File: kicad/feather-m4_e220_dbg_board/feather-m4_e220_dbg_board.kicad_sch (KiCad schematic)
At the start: 2 parts, among them U1 FEATHER_M4*, U2 E220

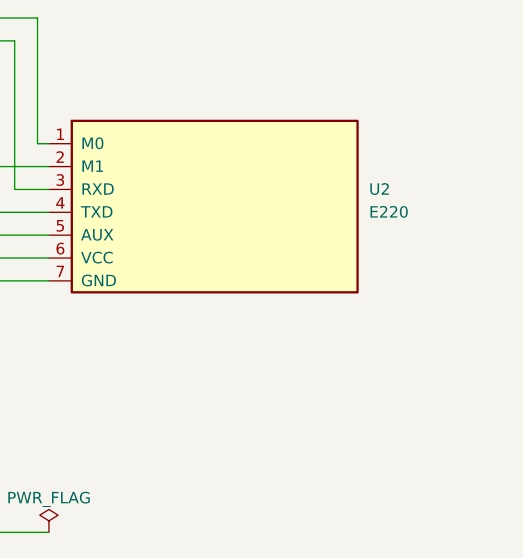
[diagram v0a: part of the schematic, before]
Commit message: Changed to place through holes for remaining E220 (as Pin8-9)
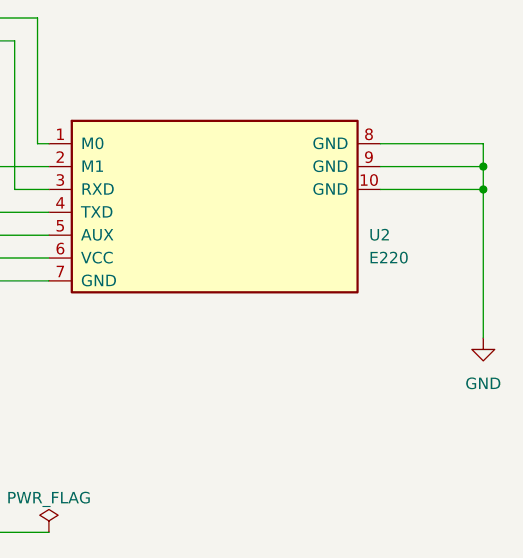
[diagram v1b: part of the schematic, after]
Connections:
- net GND: now also U2.10 (GND), U2.8 (GND), U2.9 (GND)
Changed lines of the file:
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@@
   (title_block
     (title "E220 - Feather debug board")
-    (date "2023-02-23")
-    (rev "0.1.0")
+    (date "2023-02-27")
+    (rev "0.1.1")
+  )
+  (junction (at 223.52 80.01) (diameter 0) (color 0 0 0 0)
   )
   (junction (at 165.1 120.65) (diameter 0) (color 0 0 0 0)
+  )
+  (junction (at 223.52 82.55) (diameter 0) (color 0 0 0 0)
   )
   (no_connect (at 149.86 80.01))
@@
     (stroke (width 0) (type default))
   )
+  (wire (pts (xy 223.52 82.55) (xy 223.52 99.06))
+    (stroke (width 0) (type default))
+  )
   (wire (pts (xy 173.99 63.5) (xy 173.99 77.47))
     (stroke (width 0) (type default))
@@
     (stroke (width 0) (type default))
   )
+  (wire (pts (xy 223.52 77.47) (xy 223.52 80.01))
+    (stroke (width 0) (type default))
+  )
   (wire (pts (xy 165.1 92.71) (xy 175.26 92.71))
     (stroke (width 0) (type default))
@@
     (stroke (width 0) (type default))
   )
+  (wire (pts (xy 212.09 82.55) (xy 223.52 82.55))
+    (stroke (width 0) (type default))
+  )
   (wire (pts (xy 168.91 85.09) (xy 175.26 85.09))
     (stroke (width 0) (type default))
@@
     (stroke (width 0) (type default))
   )
+  (wire (pts (xy 212.09 80.01) (xy 223.52 80.01))
+    (stroke (width 0) (type default))
+  )
   (wire (pts (xy 166.37 90.17) (xy 175.26 90.17))
     (stroke (width 0) (type default))
@@
     (stroke (width 0) (type default))
   )
+  (wire (pts (xy 212.09 77.47) (xy 223.52 77.47))
+    (stroke (width 0) (type default))
+  )
+  (wire (pts (xy 223.52 80.01) (xy 223.52 82.55))
+    (stroke (width 0) (type default))
+  )
   (wire (pts (xy 161.29 87.63) (xy 175.26 87.63))
     (stroke (width 0) (type default))
@@
         (path "/5544efbd-b141-4197-990d-fcaed2535cef"
           (reference "#FLG01") (unit 1)
+        )
+      )
+    )
+  )
+  (symbol (lib_id "power:GND") (at 223.52 99.06 0) (unit 1)
+    (in_bom yes) (on_board yes) (dnp no) (fields_autoplaced)
+    (property "Reference" "#PWR02" (at 223.52 105.41 0)
+      (effects (font (size 1.27 1.27)) hide)
+    )
+    (property "Value" "GND" (at 223.52 104.14 0)
+      (effects (font (size 1.27 1.27)))
+    )
+    (property "Footprint" "" (at 223.52 99.06 0)
+      (effects (font (size 1.27 1.27)) hide)
+    )
+    (property "Datasheet" "" (at 223.52 99.06 0)
+      (effects (font (size 1.27 1.27)) hide)
+    )
+    (pin "1")
+    (instances
+      (project "feather-m4_e220_dbg_board"
+        (path "/5544efbd-b141-4197-990d-fcaed2535cef"
+          (reference "#PWR02") (unit 1)
         )
       )
@@
   )
   (symbol (lib_id "e220:E220") (at 193.04 82.55 0) (unit 1)
-    (in_bom yes) (on_board yes) (dnp no) (fields_autoplaced)
-    (property "Reference" "U2" (at 210.82 82.55 0)
+    (in_bom yes) (on_board yes) (dnp no)
+    (property "Reference" "U2" (at 210.82 87.63 0)
       (effects (font (size 1.27 1.27)) (justify left))
     )
-    (property "Value" "E220" (at 210.82 85.09 0)
+    (property "Value" "E220" (at 210.82 90.17 0)
       (effects (font (size 1.27 1.27)) (justify left))
     )
@@
     )
     (pin "1")
+    (pin "10")
     (pin "2")
     (pin "3")
@@
     (pin "6")
     (pin "7")
-    (instances
-      (project "feather-m4_e220_dbg_board"
+    (pin "8")
+    (pin "9")
+    (instances
+      (project "feather-m4_e220_dbg_board"
